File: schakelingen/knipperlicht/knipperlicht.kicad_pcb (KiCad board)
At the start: 2 copper layers, 87.9 x 60.3 mm, 13 parts, among them Q1 BC547, Q2 BC547

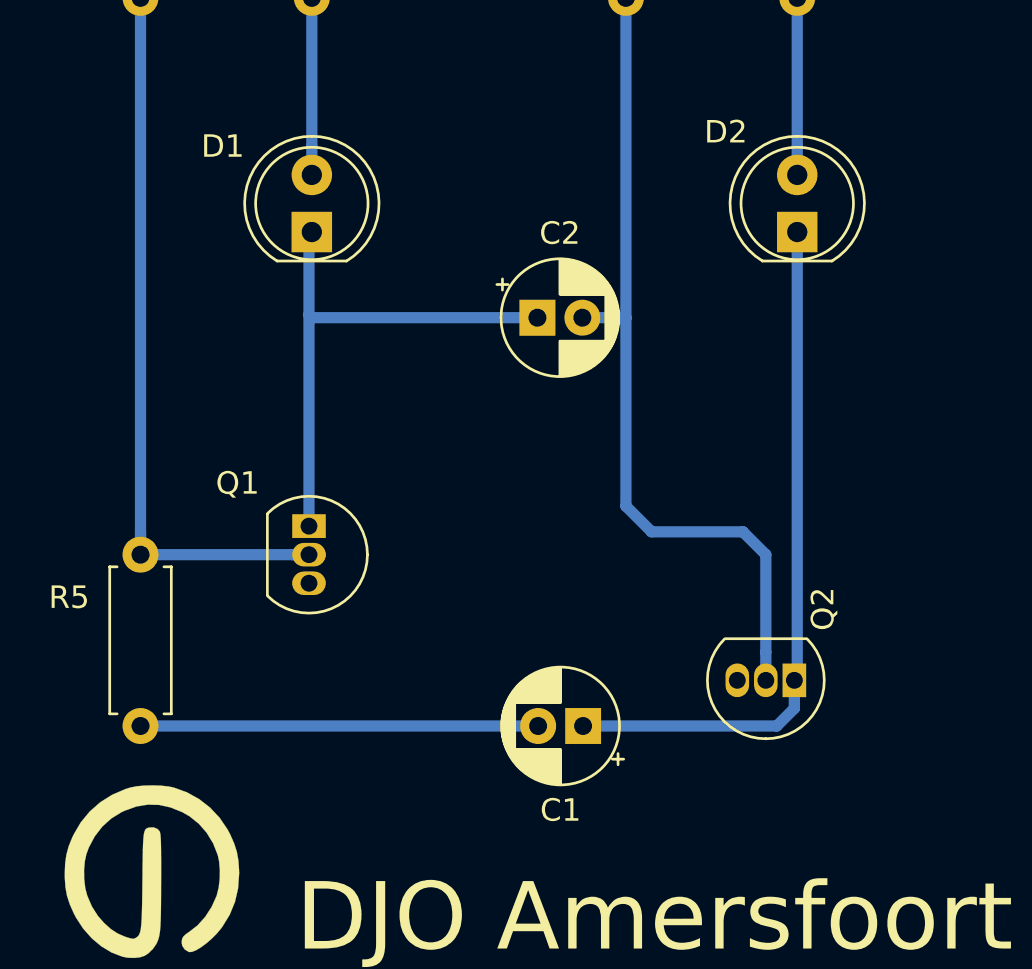
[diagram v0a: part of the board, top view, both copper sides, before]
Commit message: Footprint van transistoren knipperlicht bijgewerkt voor handsolderen
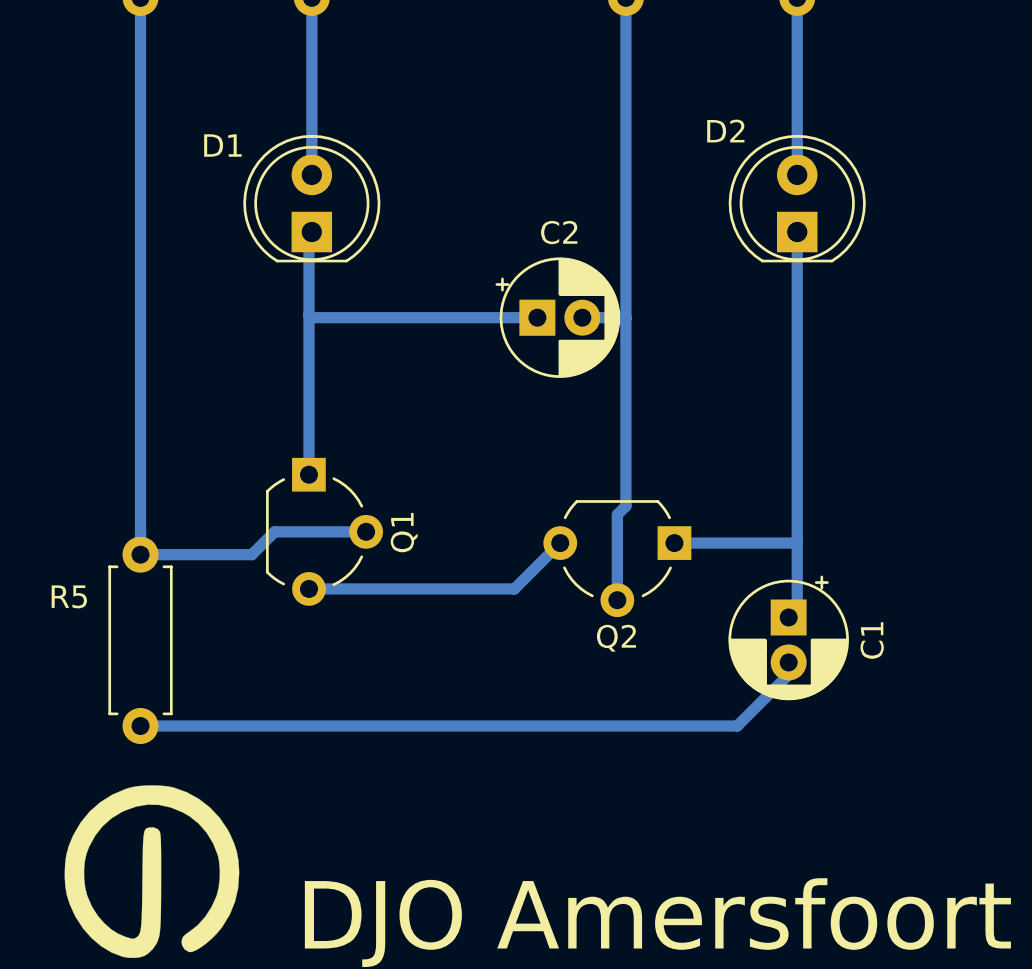
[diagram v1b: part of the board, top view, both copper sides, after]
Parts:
- Q1, Q2: footprint Package_TO_SOT_THT:TO-92_Inline -> Package_TO_SOT_THT:TO-92_Wide
- moved C1 10.3 mm to (94.0, 57.1), turned to -90 degrees
- moved Q2 8.11 mm to (88.9, 53.8)
- moved Q1 2.29 mm to (72.6, 50.8)
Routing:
- net TERUGKOPPELING: track 17.7 -> 30.3 mm
- net GND: track 0.00 -> 12.0 mm
- net Net-(C2-Pad2): track 37.2 -> 28.9 mm
- net Net-(C1-Pad1): track 31.1 -> 23.0 mm
- net Net-(Q1-Pad2): track 33.9 -> 36.4 mm
- net Net-(C2-Pad1): track 23.3 -> 21.1 mm
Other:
- net class Default removed
